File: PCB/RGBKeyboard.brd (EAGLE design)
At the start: 267.9 x 282.9 mm, 70 parts, among them P2 0475890001, U1 MSP430F5529_PN_80, U10 3341, U11 3341, U12 3341, U13 3341, U2 3341, U3 3341, U4 3341, U5 3341, U6 3341, U7 3341, U8 3341, U9 3341, Y1 ECS-40-20-5PX-TR

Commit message: Have a decent prototype but may switch LEDs
WS2812-2020s seem easier to solder but are harder to control.
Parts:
- removed C1, C2, C9: 10 uF, rcl:C0603K
- removed C10, C11: 10 pF, rcl:C0603K
- removed C12: 4.7 uF, rcl:C0603K
- removed C13: 470 nF, rcl:C0603K
- removed C14, C15, C3, C8: 100 nF, rcl:C0603K
- removed C4, C5: 32 pF, rcl:C0603K
- removed C6, C7: 220 nF, rcl:C0603K
- removed P2: 0475890001, MICRO_USB_B:MOLEX_0475890001
- removed R10: 47 k, rcl:R0603
- removed R5: 100, rcl:R0603
- removed R6, R7, R8: 27, rcl:R0603
- removed R9: 1 M, rcl:R0603
- removed S1: PTS645SM43SMTR, PTS645SM43SMTR:PTS645SM43SMTR
- removed SV2: (no value), con-lstb:MA03-1
- removed Y1: ECS-40-20-5PX-TR, ECS-40-20-5PX-TR:XTAL_ECS-40-20-5PX-TR
- added R4: 4.7k, rcl:R0603
- added SV5: (no value), con-lstb:MA03-1
- added U$13: CHERRY_MXCHERRY_MX_1_2, CHERRY_MX:CHERRY_MX_1_2
- added U$14: CHERRY_MXCHERRY_MX_1_6, CHERRY_MX:CHERRY_MX_1_6
- added U14: 3341, 3341:LED_3341
- D2: value BAS40 -> BAV21W-7-F; device diode:SOT23 -> BAV21W-7-F:SOD3715X135N
- U$10: value CHERRY_MXCHERRY_MX_1_2 -> CHERRY_MX; device CHERRY_MX:CHERRY_MX_1_2 -> CHERRY_MX:CHERRY_MX
- U$11: value CHERRY_MXCHERRY_MX_1_6 -> CHERRY_MX; device CHERRY_MX:CHERRY_MX_1_6 -> CHERRY_MX:CHERRY_MX
- U1: value MSP430F5529_PN_80 -> 3341; device MSP430F5529_80:PN80 -> 3341:LED_3341
- moved D2 199.6 mm to (146.1, 31.8), turned to 270 degrees
- moved U1 176.5 mm to (3.81, -5.08), flipped to the top
- moved SV1 156.2 mm to (146.1, 71.1), flipped to the top, turned to 90 degrees
- moved D14 139.6 mm to (63.5, 31.8)
- moved SV4 74.8 mm to (5.08, 92.7), turned to 270 degrees
- moved U12 60.3 mm to (67.3, 38.1), turned to 0 degrees
- moved U6 44.9 mm to (88.9, 59.7)
- moved U7 44.9 mm to (67.3, 59.7)
- moved R2 44.9 mm to (100.3, 77.5), turned to 270 degrees
- moved R3 44.9 mm to (100.3, 55.9), turned to 90 degrees
- moved U8 44.9 mm to (45.7, 59.7)
- moved SV3 34.9 mm to (55.9, 108.0)
- moved D12 32.6 mm to (66.0, 54.6)
- moved D6 32.6 mm to (66.0, 97.8)
- moved D8 32.6 mm to (66.0, 76.2)
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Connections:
- removed net N$31: C13.1, U1.20
- removed net N$32: D14.A, SV1.4
- removed net N$7: P2.4
- removed net N$8: P2.2, R6.2
- removed net PU.0/DP: C10.1, R7.1, R8.2, R9.2, U1.62
- removed net PU.1/DM: C11.1, R6.1, U1.64
- removed net PUR: R5.1, R8.1, U1.63
- removed net RST: R10.2, SV1.3, U1.76
- removed net TST: SV1.2
- removed net V18: C7.1, U1.67
- removed net VBUS: C12.1, D14.C, D2.3, U1.65
- removed net VSSU: C6.2, C7.2, C9.2, U1.61
- removed net VUSB: C6.1, C8.1, C9.1, S1.3, S1.4
- removed net XT2IN: C5.1, U1.69, Y1.1
- removed net XT2OUT: C4.1, U1.70, Y1.2
- new net CKO2: U1.5, U13.2
- new net ROW3: D14.C, D2.C, R4.2, SV1.1
- new net SDO2: U1.4, U13.3
- net COL0: now also U$13.2; no longer U1.27
- net COL1: now also U$14.2; no longer U1.26
- net COL2: no longer U1.25
- net COL3: no longer U1.24
- net DVCC: now also U1.1, U1.8, U14.1, U14.8; no longer C1.1, C14.1, C15.1, C2.1, C3.1, R10.1, U1.11, U1.18, U1.50, U1.66
- net GND: now also R4.1, U1.6, U1.7, U14.6, U14.7; no longer C1.2, C10.2, C11.2, C12.2, C13.2, C14.2, C15.2, C2.2, C3.2, C4.2, C5.2, P2.5, R9.1, SV1.1, U1.14, U1.19, U1.49, U1.68
- net N$10: now also U1.3, U14.4; no longer D2.1, P2.1
- net N$4: now also D2.A, U$13.1; no longer R5.2, S1.1, S1.2
- net N$5: now also D14.A, U$14.1; no longer C8.2
- net N$9: now also U1.2, U14.5; no longer P2.3, R7.2
- net ROW0: now also SV1.4; no longer SV2.3, U1.23
- net ROW1: now also SV1.3; no longer SV2.2, U1.22
- net ROW2: now also SV1.2; no longer SV2.1, U1.21
- net UCA0CLK: now also SV5.3; no longer U1.36
- net UCA0SIMO: now also SV5.2; no longer U1.40
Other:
- board size 267.9 x 282.9 mm -> 171.4 x 114 mm

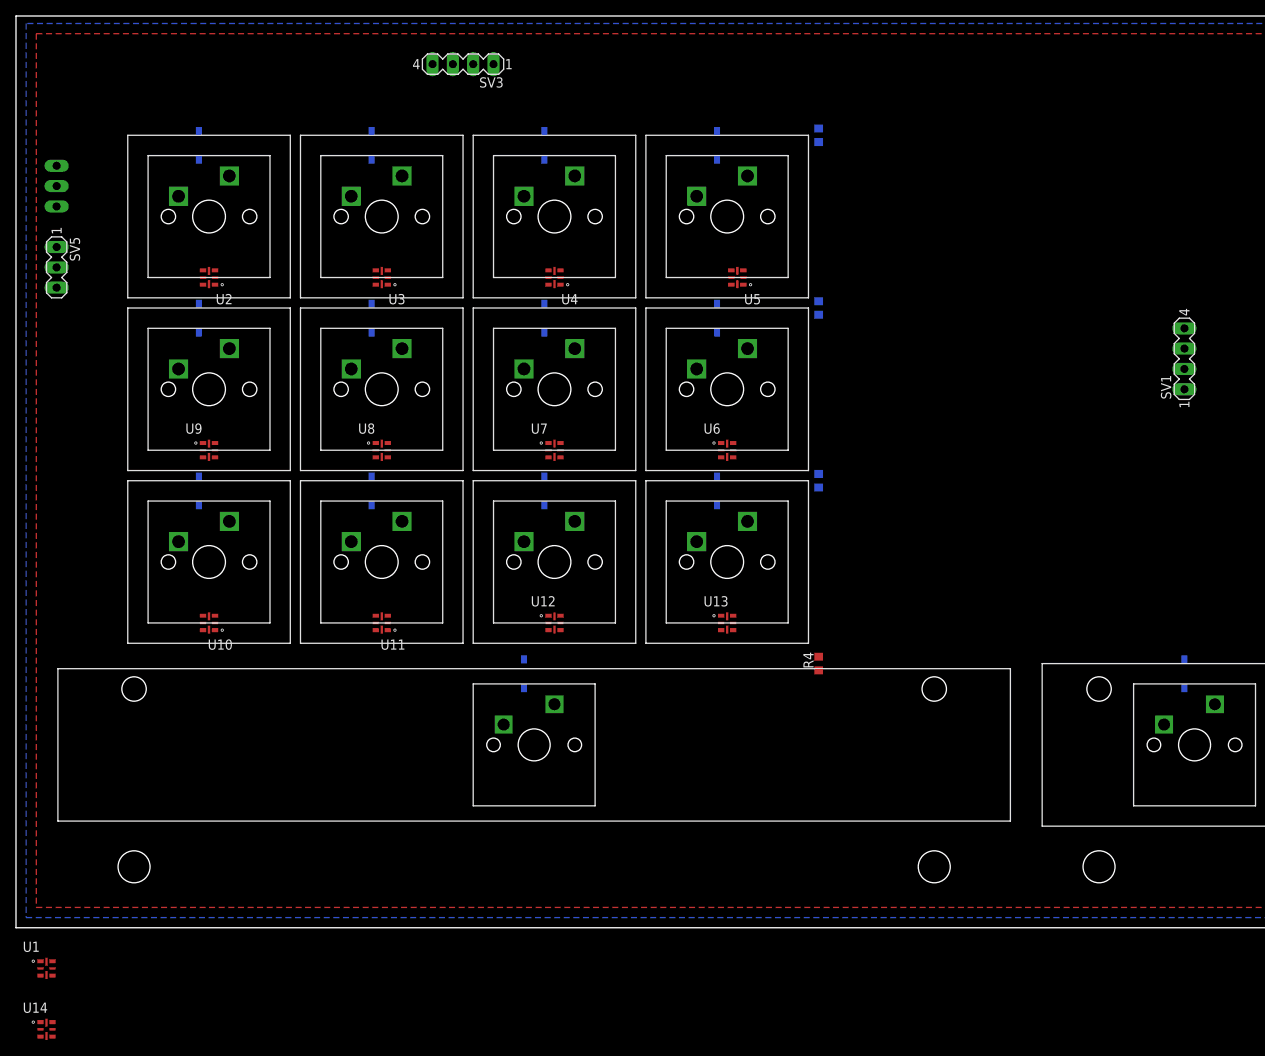
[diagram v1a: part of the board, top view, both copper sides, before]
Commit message: Schematic and Board for first prototype
Ended up removing the LEDs entirely (rip) because
there was too much uncertainty with dimensions
and routing was annoying
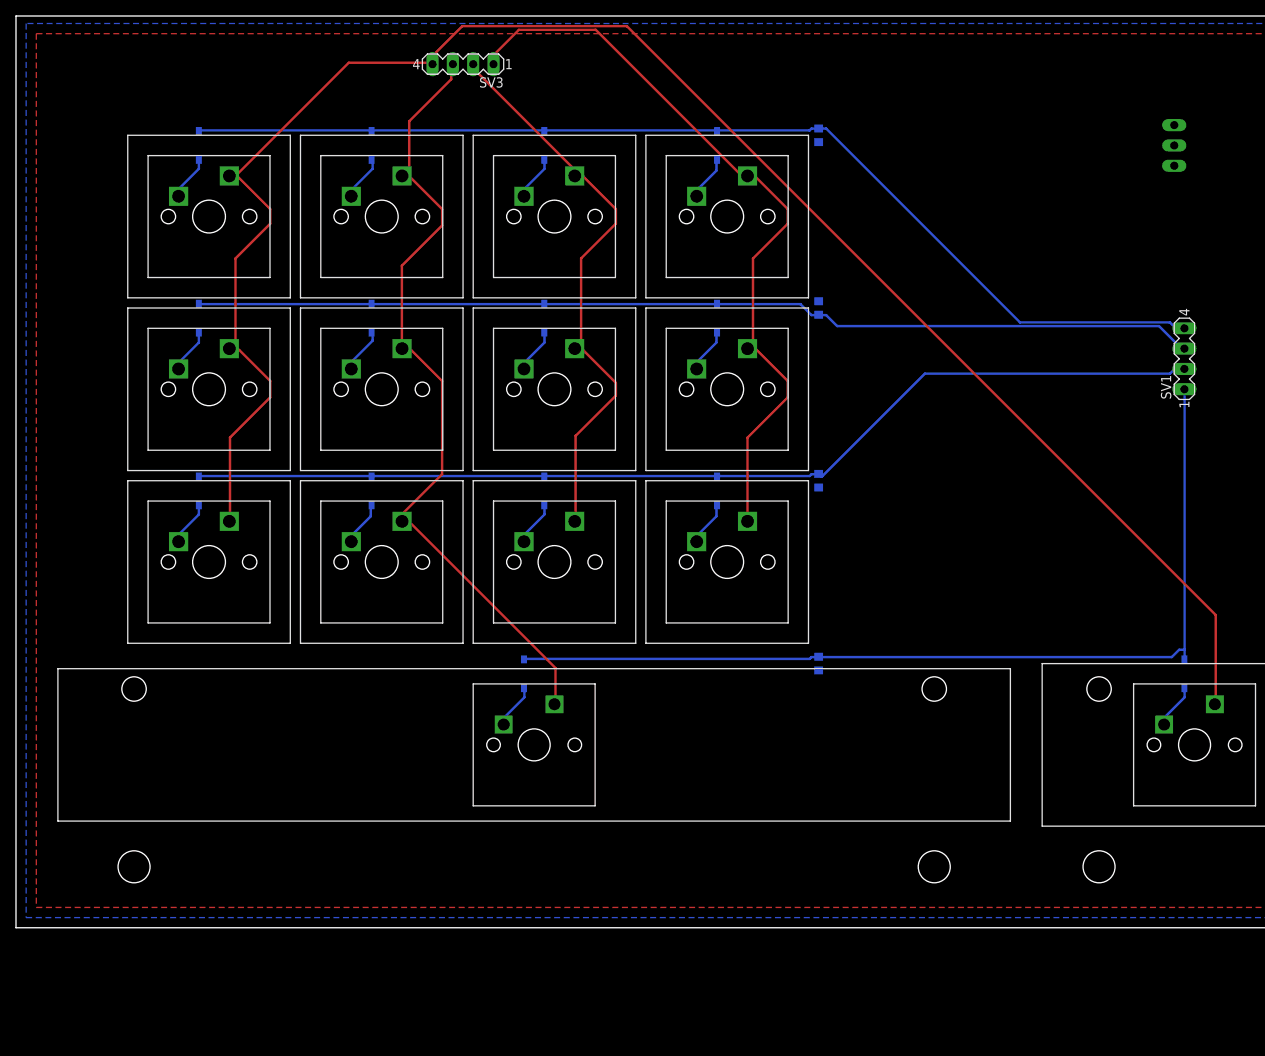
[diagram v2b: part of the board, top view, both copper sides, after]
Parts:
- removed SV5: (no value), con-lstb:MA03-1
- removed U1, U10, U11, U12, U13, U14, U2, U3, U4, U5, U6, U7, U8, U9: 3341, 3341:LED_3341
- moved SV4 139.8 mm to (144.8, 97.8)
- flipped R4 to the bottom
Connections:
- removed net CKO0: U5.2, U6.5
- removed net CKO1: U10.5, U9.2
- removed net CKO2: U1.5, U13.2
- removed net N$10: U1.3, U14.4
- removed net N$13: U2.2, U3.5
- removed net N$14: U2.3, U3.4
- removed net N$15: U3.2, U4.5
- removed net N$16: U3.3, U4.4
- removed net N$17: U4.2, U5.5
- removed net N$18: U4.3, U5.4
- removed net N$19: U6.2, U7.5
- removed net N$20: U6.3, U7.4
- removed net N$21: U7.2, U8.5
- removed net N$22: U7.3, U8.4
- removed net N$23: U8.2, U9.5
- removed net N$24: U8.3, U9.4
- removed net N$25: U10.2, U11.5
- removed net N$26: U10.3, U11.4
- removed net N$27: U11.2, U12.5
- removed net N$28: U11.3, U12.4
- removed net N$29: U12.2, U13.5
- removed net N$30: U12.3, U13.4
- removed net N$9: U1.2, U14.5
- removed net SDO0: U5.3, U6.4
- removed net SDO1: U10.4, U9.3
- removed net SDO2: U1.4, U13.3
- removed net UCA0CLK: SV5.3, U2.5
- removed net UCA0SIMO: SV5.2, U2.4
- net DVCC: no longer U1.1, U1.8, U10.1, U10.8, U11.1, U11.8, U12.1, U12.8, U13.1, U13.8, U14.1, U14.8, U2.1, U2.8, U3.1, U3.8, U4.1, U4.8, U5.1, U5.8, U6.1, U6.8, U7.1, U7.8, U8.1, U8.8, U9.1, U9.8
- net GND: no longer U1.6, U1.7, U10.6, U10.7, U11.6, U11.7, U12.6, U12.7, U13.6, U13.7, U14.6, U14.7, U2.6, U2.7, U3.6, U3.7, U4.6, U4.7, U5.6, U5.7, U6.6, U6.7, U7.6, U7.7, U8.6, U8.7, U9.6, U9.7
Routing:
- net COL0: track 0.00 -> 227.1 mm
- net ROW0: track 0.00 -> 133.9 mm
- net ROW2: track 0.00 -> 129.1 mm
- net ROW1: track 0.00 -> 125.6 mm
- net ROW3: track 0.00 -> 116.9 mm
- net COL1: track 0.00 -> 100.6 mm
- net COL3: track 0.00 -> 95.2 mm
- net COL2: track 0.00 -> 72.6 mm
- net N$6: track 0.00 -> 5.78 mm
- net N$2: track 0.00 -> 5.73 mm
- net N$3: track 0.00 -> 5.69 mm
- net N$5: track 0.00 -> 5.65 mm
- net N$11: track 0.00 -> 5.65 mm
- net N$33: track 0.00 -> 5.64 mm
- net N$12: track 0.00 -> 5.64 mm
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
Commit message: New board design for 16 percent
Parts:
- removed D14, D2: BAV21W-7-F, BAV21W-7-F:SOD3715X135N
- removed R1, R2, R3, R4: 4.7k, rcl:R0603
- removed SV1, SV3: (no value), con-lstb:MA04-1
- removed SV4: (no value), con-lstb:MA03-1
- added C1, C2, C3, C4: .1uF, rcl:C0805
- added C5, C6: 4.7uF, rcl:C0805
- added C7, C8: 22pF, rcl:C0805
- added D16, D17, D18, D19: BAV21W-7-F, BAV21W-7-F:SOD3715X135N
- added J1: UX60SC-MB-5S8, UX60SC-MB-5S8:HIROSE_UX60SC-MB-5S8
- added R5, R6: 10k, rcl:R0805
- added R7, R8: 22, rcl:R0805
- added SW1: TL3342F160QG/TR, TL3342F160QG_TR:SW_TL3342F160QG/TR
- added U$15: CHERRY_MXCHERRY_MX_1_2, CHERRY_MX:CHERRY_MX_1_2
- added U$16, U$17, U$18, U$19: CHERRY_MX, CHERRY_MX:CHERRY_MX
- added U1: ATMEGA32U4-AUR, ATMEGA32U4-AUR:QFP80P1200X1200X120-44N
- added X1: FA-238, FA-238:OSCCC320X250X70-4N
- U$14: value CHERRY_MXCHERRY_MX_1_6 -> CHERRY_MXCHERRY_MX_1_2; device CHERRY_MX:CHERRY_MX_1_6 -> CHERRY_MX:CHERRY_MX_1_2
- moved U$13 91.2 mm to (57.1, 9.53)
- moved U$14 47.6 mm to (19.1, 9.53)
- moved D3 42.5 mm to (22.2, 61.6), turned to 90 degrees
- moved D1 41.2 mm to (3.17, 61.6), turned to 90 degrees
- moved D7 39.0 mm to (73.0, 61.6), turned to 90 degrees
- moved D11 38.2 mm to (22.2, 23.5), turned to 90 degrees
- moved D6 38.2 mm to (54.0, 61.6), turned to 90 degrees
- moved D10 36.8 mm to (3.17, 23.5), turned to 90 degrees
- moved D13 34.4 mm to (73.0, 23.5), turned to 90 degrees
- moved D12 33.4 mm to (54.0, 23.5), turned to 90 degrees
- moved D5 32.3 mm to (22.2, 52.7)
- moved U$12 31.4 mm to (66.7, 66.7)
- moved D4 30.7 mm to (3.17, 52.7)
- moved U$10 29.7 mm to (66.7, 47.6)
- moved U$7 29.7 mm to (47.6, 66.7)
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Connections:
- removed net COL2: SV3.2, U$7.2, U$8.2, U$9.2
- removed net DVCC: SV4.3
- removed net N$4: D2.A, U$13.1
- removed net N$5: D14.A, U$14.1
- new net N$10: R6.2, U1.33
- new net N$13: J1.1, U1.2
- new net N$14: R7.2, U1.3
- new net N$15: J1.2, R7.1
- new net N$16: R8.2, U1.4
- new net N$17: J1.3, R8.1
- new net N$18: D17.A, U$14.1, U$18.1
- new net N$19: D19.A, U$16.1
- new net N$20: D16.A, U$13.1, U$17.1
- new net N$21: D18.A, U$15.1, U$19.1
- new net N$22: U$10.2, U$11.2, U$12.2, U$16.2
- new net N$7: C8.2, U1.17, X1.3
- new net N$8: C7.2, U1.16, X1.1
- new net N$9: R5.1, SW1.1, SW1.2, U1.13
- new net UCAP: C6.2, U1.6
- new net VCC: C1.1, C2.1, C3.1, C4.1, C5.1, R5.2, U1.14, U1.24, U1.34, U1.44, U1.7
- net COL0: now also U$17.2; no longer SV3.4
- net COL1: now also U$18.2; no longer SV3.3
- net COL3: now also U$15.2, U$19.2, U$7.2, U$8.2, U$9.2; no longer SV3.1, U$10.2, U$11.2, U$12.2
- net GND: now also C1.2, C2.2, C3.2, C4.2, C5.2, C6.1, C7.1, C8.1, J1.5, J1.S1, J1.S2, J1.S3, J1.S4, R6.1, SW1.3, SW1.4, U1.15, U1.23, U1.35, U1.43, U1.5, X1.2, X1.4; no longer R1.1, R2.1, R3.1, R4.1, SV4.2
- net ROW0: no longer R1.2, SV1.4
- net ROW1: no longer R2.2, SV1.3
- net ROW2: no longer R3.2, SV1.2
- net ROW3: now also D16.C, D17.C, D18.C, D19.C; no longer D14.C, D2.C, R4.2, SV1.1
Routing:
- net COL0: track 227.1 -> 0.00 mm
- net ROW0: track 133.9 -> 0.00 mm
- net ROW2: track 129.1 -> 0.00 mm
- net ROW1: track 125.6 -> 0.00 mm
- net ROW3: track 116.9 -> 0.00 mm
- net COL1: track 100.6 -> 0.00 mm
- net COL3: track 95.2 -> 0.00 mm
- net COL2: track 72.6 -> 0.00 mm
- net N$6: track 5.78 -> 0.00 mm
- net N$2: track 5.73 -> 0.00 mm
- net N$3: track 5.69 -> 0.00 mm
- net N$5: track 5.65 -> 0.00 mm
- net N$11: track 5.65 -> 0.00 mm
- net N$33: track 5.64 -> 0.00 mm
- net N$12: track 5.64 -> 0.00 mm
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- removed copper zone on layer 1, net GND
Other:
- board size 171.4 x 114 mm -> 76.2 x 76.5 mm

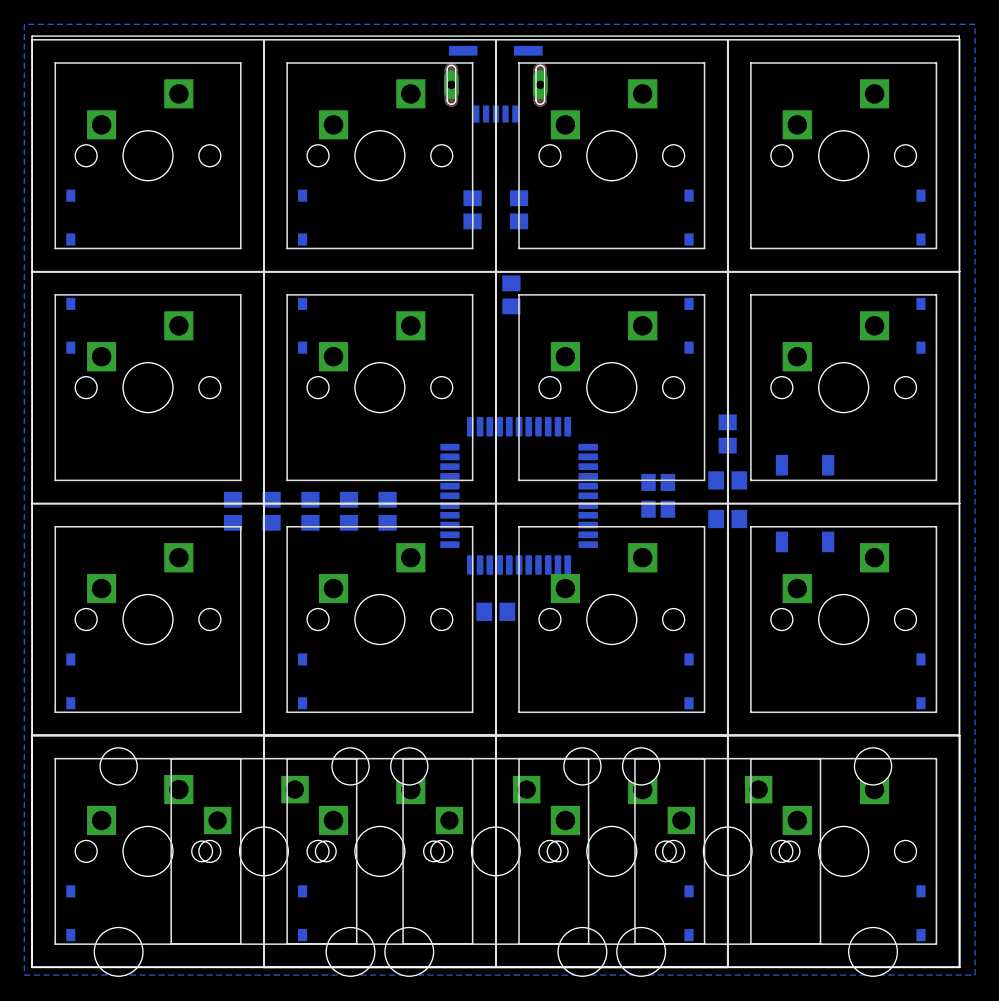
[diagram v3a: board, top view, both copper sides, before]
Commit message: Make holes smaller. 19mm key spacing
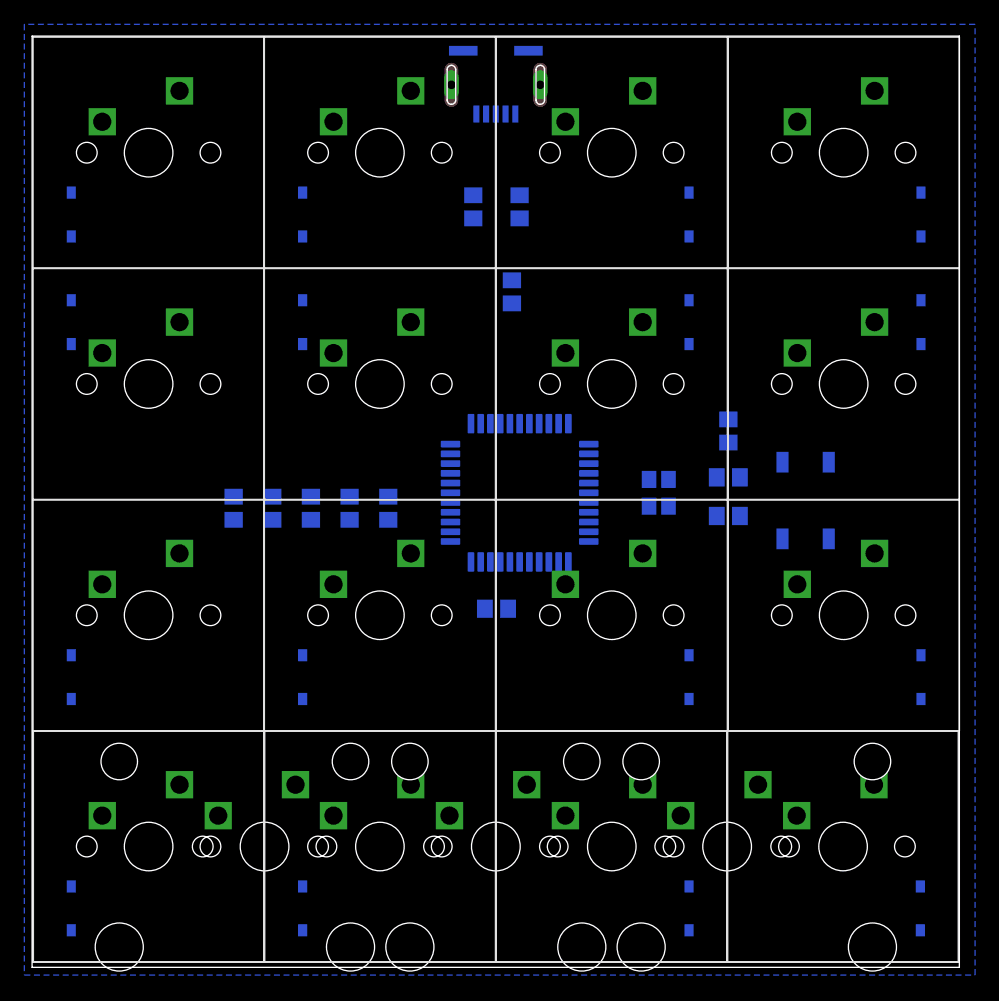
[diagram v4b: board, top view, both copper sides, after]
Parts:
- moved D19 0.40 mm to (73.0, 4.84)
- moved U$14 0.40 mm to (19.1, 9.93)
- moved U$18 0.40 mm to (9.57, 9.93)
- moved U$13 0.40 mm to (57.1, 9.93)
- moved U$16 0.40 mm to (66.6, 9.93)
- moved D17 0.40 mm to (3.23, 4.84)
- moved U$15 0.40 mm to (38.1, 9.93)
- moved U$17 0.40 mm to (47.6, 9.93)
- moved U$19 0.40 mm to (28.6, 9.93)
- moved D16 0.40 mm to (22.2, 4.84)
- moved D18 0.40 mm to (54.0, 4.84)
- moved U$3 0.35 mm to (9.57, 28.9)
- moved D10 0.35 mm to (3.23, 23.8)
- moved U$11 0.35 mm to (66.7, 28.9)
- moved U$6 0.35 mm to (28.6, 28.9)
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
